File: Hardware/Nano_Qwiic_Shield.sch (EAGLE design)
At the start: 16 parts, among them J1 QWIIC_RIGHT_ANGLE, J2 QWIIC_RIGHT_ANGLE, J3 Vertical Qwiic Connector, J4 Vertical Qwiic Connector, U1 NANO_FOOTPRINT

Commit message: Initial commit/run of checklist
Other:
- note added: "Nano Footprint VCC: 3.3V (Qwiic)"
- note added: "v10"
- note removed: "Nano Footprint VCC: 2.7-3.6V"
- note removed: "v01"
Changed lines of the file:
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@@
 <wire x1="147.32" y1="35.56" x2="147.32" y2="185.42" width="0.2032" layer="97" style="longdash"/>
 <text x="166.37" y="11.176" size="2.54" layer="94" font="vector">Andy England</text>
-<text x="236.22" y="7.62" size="2.54" layer="94" font="vector">v01</text>
+<text x="236.22" y="7.62" size="2.54" layer="94" font="vector">v10</text>
 <text x="2.54" y="177.8" size="2.54" layer="94" font="vector">Nano Footprint
-VCC: 2.7-3.6V</text>
+VCC: 3.3V (Qwiic)</text>
 <text x="149.86" y="177.8" size="2.54" layer="94" font="vector">Qwiic Connections</text>
 <text x="10.16" y="121.92" size="1.27" layer="94" font="vector">Connect the I2C jumpers if your slave

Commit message: post review changes
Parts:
- FD1, FD2, FD3, FD4: value FIDUCIAL0.2MM -> FIDUCIAL1X2; device SparkFun-Aesthetics:FIDUCIAL0.2MM -> SparkFun-Aesthetics:FIDUCIAL1X2
- renumbered U1 to J5
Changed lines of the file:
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@@
 <parts>
 <part name="FRAME1" library="SparkFun-Aesthetics" deviceset="FRAME-LETTER" device=""/>
-<part name="U1" library="SparkFun-Boards" deviceset="NANO_FOOTPRINT" device=""/>
+<part name="J5" library="SparkFun-Boards" deviceset="NANO_FOOTPRINT" device=""/>
 <part name="SUPPLY1" library="SparkFun-PowerSymbols" deviceset="3.3V" device=""/>
 <part name="GND1" library="SparkFun-PowerSymbols" deviceset="GND" device=""/>
@@
 <part name="LOGO2" library="SparkFun-Aesthetics" deviceset="SFE_LOGO_NAME_FLAME" device=".1_INCH"/>
 <part name="LOGO3" library="SparkFun-Aesthetics" deviceset="SFE_LOGO_NAME_FLAME" device=".1_INCH" value="SFE_LOGO_NAME_FLAME.1_INCH"/>
-<part name="FD1" library="SparkFun-Aesthetics" deviceset="FIDUCIAL" device="0.2MM"/>
-<part name="FD2" library="SparkFun-Aesthetics" deviceset="FIDUCIAL" device="0.2MM"/>
-<part name="FD3" library="SparkFun-Aesthetics" deviceset="FIDUCIAL" device="0.2MM"/>
-<part name="FD4" library="SparkFun-Aesthetics" deviceset="FIDUCIAL" device="0.2MM"/>
+<part name="FD1" library="SparkFun-Aesthetics" deviceset="FIDUCIAL" device="1X2" value="FIDUCIAL1X2"/>
+<part name="FD2" library="SparkFun-Aesthetics" deviceset="FIDUCIAL" device="1X2" value="FIDUCIAL1X2"/>
+<part name="FD3" library="SparkFun-Aesthetics" deviceset="FIDUCIAL" device="1X2" value="FIDUCIAL1X2"/>
+<part name="FD4" library="SparkFun-Aesthetics" deviceset="FIDUCIAL" device="1X2" value="FIDUCIAL1X2"/>
 </parts>
 <sheets>
@@
 <instance part="FRAME1" gate="G$1" x="0" y="0"/>
 <instance part="FRAME1" gate="V" x="147.32" y="0"/>
-<instance part="U1" gate="G$1" x="76.2" y="106.68"/>
+<instance part="J5" gate="G$1" x="76.2" y="106.68"/>
 <instance part="SUPPLY1" gate="G$1" x="60.96" y="129.54"/>
 <instance part="GND1" gate="1" x="60.96" y="114.3"/>
@@
 <net name="3.3V" class="0">
 <segment>
-<pinref part="U1" gate="G$1" pin="3V3"/>
+<pinref part="J5" gate="G$1" pin="3V3"/>
 <wire x1="63.5" y1="124.46" x2="60.96" y2="124.46" width="0.1524" layer="91"/>
 <wire x1="60.96" y1="124.46" x2="60.96" y2="129.54" width="0.1524" layer="91"/>
@@
 <net name="GND" class="0">
 <segment>
-<pinref part="U1" gate="G$1" pin="GND"/>
+<pinref part="J5" gate="G$1" pin="GND"/>
 <wire x1="63.5" y1="119.38" x2="60.96" y2="119.38" width="0.1524" layer="91"/>
 <pinref part="GND1" gate="1" pin="GND"/>
@@
 <net name="SCL" class="0">
 <segment>
-<pinref part="U1" gate="G$1" pin="A5/SCL"/>
+<pinref part="J5" gate="G$1" pin="A5/SCL"/>
 <wire x1="63.5" y1="104.14" x2="60.96" y2="104.14" width="0.1524" layer="91"/>
 <wire x1="60.96" y1="104.14" x2="53.34" y2="104.14" width="0.1524" layer="91"/>
@@
 <net name="SDA" class="0">
 <segment>
-<pinref part="U1" gate="G$1" pin="A4/SDA"/>
+<pinref part="J5" gate="G$1" pin="A4/SDA"/>
 <wire x1="63.5" y1="101.6" x2="60.96" y2="101.6" width="0.1524" layer="91"/>
 <wire x1="35.56" y1="101.6" x2="38.1" y2="101.6" width="0.1524" layer="91"/>

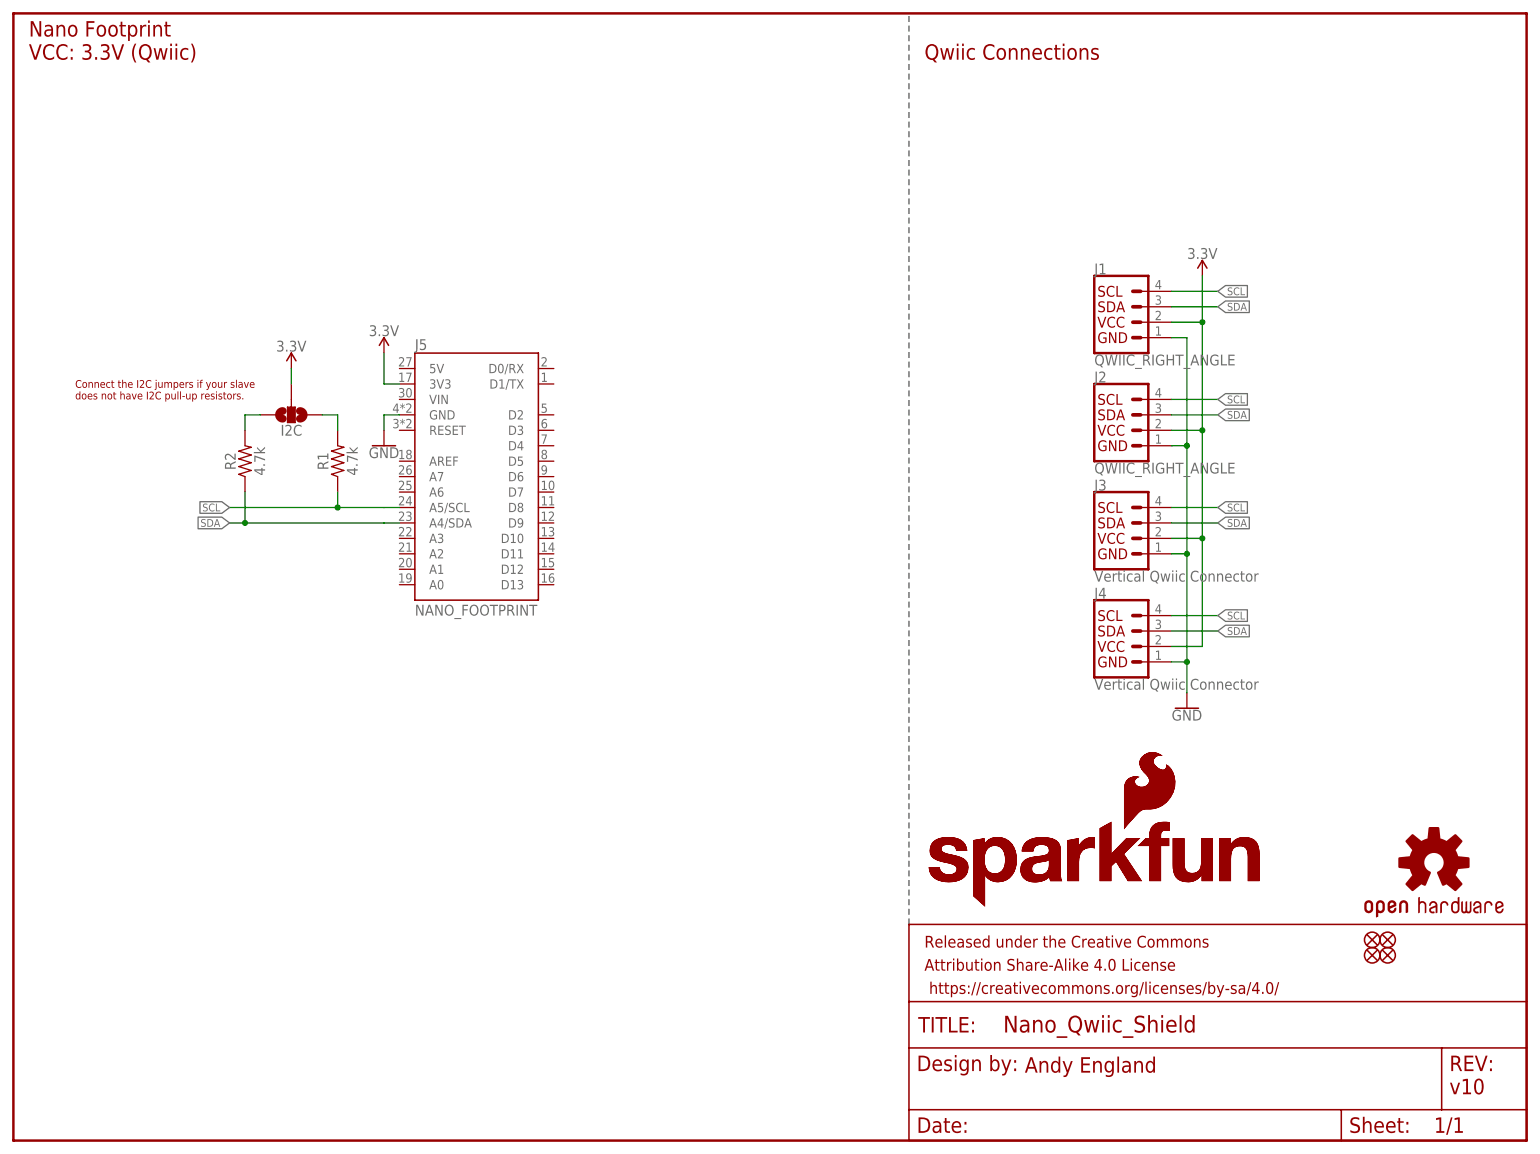
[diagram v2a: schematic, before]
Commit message: adding conversion circuitry
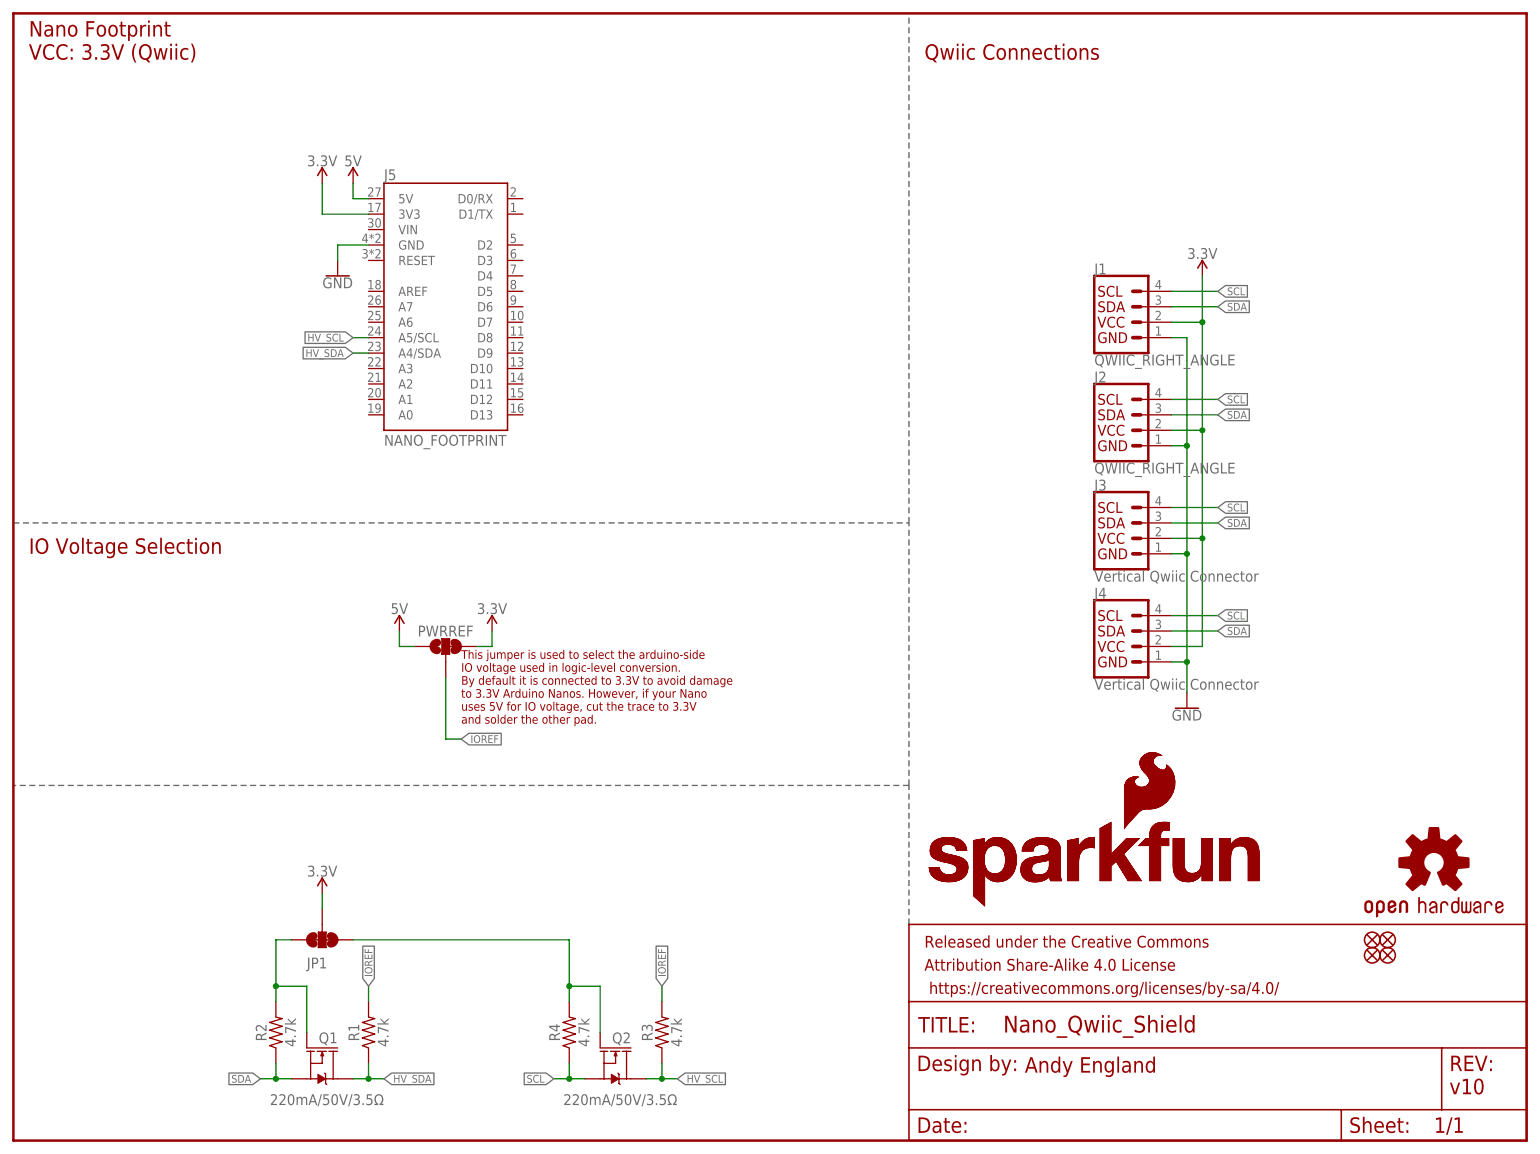
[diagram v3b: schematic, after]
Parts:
- removed I2C: JUMPER-SMT_3_NO_NO-SILK, SparkFun-Jumpers:JUMPER-SMT_3_NO_NO-SILK
- added JP1: JUMPER-SMT_3_2-NC_TRACE_NO-SILK, SparkFun-Jumpers:JUMPER-SMT_3_2-NC_TRACE_NO-SILK
- added PWRREF: JUMPER-SMT_3_1-NC_TRACE_NO-SILK, SparkFun-Jumpers:JUMPER-SMT_3_1-NC_TRACE_NO-SILK
- added Q1, Q2: 220mA/50V/3.5Ω, SparkFun-DiscreteSemi:MOSFET-NCH-BSS138
- added R3, R4: 4.7k, SparkFun-Resistors:4.7KOHM-0603-1/10W-1%
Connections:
- removed net N$1: I2C.3, R2.2
- removed net N$2: I2C.1, R1.2
- new net 5V: J5.5V, PWRREF.1
- new net HV_SCL: J5.A5/SCL, Q2.D, R3.1
- new net HV_SDA: J5.A4/SDA, Q1.D, R1.1
- new net IOREF: PWRREF.2, R1.2, R3.2
- new net SCLJUMP: JP1.1, Q2.G, R4.2
- new net SDAJUMP: JP1.3, Q1.G, R2.2
- net 3.3V: now also JP1.2, PWRREF.3; no longer I2C.2
- net SCL: now also Q2.S, R4.1; no longer J5.A5/SCL, R1.1
- net SDA: now also Q1.S; no longer J5.A4/SDA
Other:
- note added: "IO Voltage Selection"
- note added: "This jumper is used to select the arduino-side IO voltage used in logic-level conversion. By default it is connected to 3.3V to avoid damage to 3.3V Arduino Nanos. However, if your Nano uses 5V for IO voltage, cut the trace to 3.3V and solder the other pad."
- note removed: "Connect the I2C jumpers if your slave does not have I2C pull-up resistors."
- moved on the sheet: J5, R1, R2
